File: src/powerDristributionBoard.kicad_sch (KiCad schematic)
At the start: 20 parts

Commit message: test
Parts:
- added D2: Light-Emitting Diode, symbol Simulation Generic Components:LED

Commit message: Test Commit
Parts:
- removed D1, D2: Light-Emitting Diode, symbol Simulation Generic Components:LED
- removed TVS3: Zener Diode, symbol Simulation Generic Components:Zener Diode
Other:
- removed sheet 26 to 12V(5A)1
- note added: "THIS SENTENCE IS BEING USED AS A TEST"
- moved on the sheet: D?, ESD1, ESD2, F?, M?, R1, R17, R18, R2, R9, TVS1, TVS2

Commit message: Testing to see if my updates get pushed to the repository.
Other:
- note added: "-Jonathan V"
- note added: "If you're reading this, that means my attempt to push updates into the repository was successful"
- note added: "P.S. Issac's the goat"
- note removed: "THIS SENTENCE IS BEING USED AS A TEST"
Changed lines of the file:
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@@
 	(generator_version "10.0")
 	(paper "A")
-	(text "THIS SENTENCE IS BEING USED AS A TEST"
+	(text "If you're reading this, that means my attempt to push updates into the repository was successful\n"
 		(exclude_from_sim no)
-		(at 86.868 45.72 0)
+		(at 121.158 26.416 0)
 		(effects
 			(font
@@
 			)
 		)
+	)
+	(text "-Jonathan V"
+		(exclude_from_sim no)
+		(at 214.63 34.036 0)
+		(effects
+			(font
+				(size 2.54 2.54)
+			)
+		)
+	)
+	(text "P.S. Issac's the goat"
+		(exclude_from_sim no)
+		(at 251.714 181.356 0)
+		(effects
+			(font
+				(size 1.27 1.27)
+			)
+		)

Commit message: Update power distribution board
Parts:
- removed D?: Light-Emitting Diode, symbol Simulation Generic Components:LED
- removed F?: MF-MSMF050-2, powerDristributionBoard-import-fps:BOUR-MF-MSMF050-2_V, symbol Autonomous Vehicle Lab:PPTC-2
- removed M?: P-channel Power MOSFET VDMOS Model, symbol Simulation Generic Components:MOSFET P-ch VDMOS
- removed R1, R2: Resistor, symbol Simulation Generic Components:Resistor
- removed TVS1: Zener Diode, symbol Simulation Generic Components:Zener Diode
- added D1: TVS, symbol Device:D_Zener
- added D2: LED, symbol Device:LED
- added F1: RTC, symbol Device:Fuse_Small
- added R1: Find Val, symbol Device:R_Small_US
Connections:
- net 26 to 12V(5A)/Vin+: now also D1.1 (K), F1.2, R1.1
- net GND: now also D1.2 (A), D2.1 (K)
- net Protection Circuit/Vout: now also F1.1
- new net: D2.2 (A), R1.2
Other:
- note removed: "-Jonathan V"
- note removed: "P.S. Issac's the goat"

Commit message: Added diode
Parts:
- added D3: TVS, symbol Device:D_Zener
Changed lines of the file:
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@@
+	)
+	(symbol
+		(lib_id "Device:D_Zener")
+		(at 68.58 127 270)
+		(unit 1)
+		(body_style 1)
+		(exclude_from_sim no)
+		(in_bom yes)
+		(on_board yes)
+		(in_pos_files yes)
+		(dnp no)
+		(fields_autoplaced yes)
+		(property "Reference" "D3"
+			(at 71.12 125.7299 90)
+			(show_name no)
+			(do_not_autoplace no)
+			(effects
+				(font
+					(size 1.27 1.27)
+				)
+				(justify left)
+			)
+		)
+		(property "Value" "TVS"
+			(at 71.12 128.2699 90)
+			(show_name no)
+			(do_not_autoplace no)
+			(effects
+				(font
+					(size 1.27 1.27)
+				)
+				(justify left)
+			)
+		)
+		(property "Footprint" ""
+			(at 68.58 127 0)
+			(hide yes)
+			(show_name no)
+			(do_not_autoplace no)
+			(effects
+				(font
+					(size 1.27 1.27)
+				)
+			)
+		)
+		(property "Datasheet" ""
+			(at 68.58 127 0)
+			(hide yes)
+			(show_name no)
+			(do_not_autoplace no)
+			(effects
+				(font
+					(size 1.27 1.27)
+				)
+			)
+		)
+		(property "Description" "Zener diode"
+			(at 68.58 127 0)
+			(hide yes)
+			(show_name no)
+			(do_not_autoplace no)
+			(effects
+				(font
+					(size 1.27 1.27)
+				)
+			)
+		)
+		(pin "1"
+		)
+		(pin "2"
+		)
+		(instances
+			(project "powerDristributionBoard"
+				(path "/d5fc2ae9-f21d-48b0-bd61-912ade1f672f"
+					(reference "D3")
+					(unit 1)
+				)
+			)
+		)
 	)
 	(symbol

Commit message: Added two diodes
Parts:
- added D4, D5: LED, symbol Device:LED
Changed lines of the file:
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@@
+	)
+	(symbol
+		(lib_id "Device:LED")
+		(at 106.68 124.46 90)
+		(unit 1)
+		(body_style 1)
+		(exclude_from_sim no)
+		(in_bom yes)
+		(on_board yes)
+		(in_pos_files yes)
+		(dnp no)
+		(fields_autoplaced yes)
+		(property "Reference" "D4"
+			(at 110.49 124.7774 90)
+			(show_name no)
+			(do_not_autoplace no)
+			(effects
+				(font
+					(size 1.27 1.27)
+				)
+				(justify right)
+			)
+		)
+		(property "Value" "LED"
+			(at 110.49 127.3174 90)
+			(show_name no)
+			(do_not_autoplace no)
+			(effects
+				(font
+					(size 1.27 1.27)
+				)
+				(justify right)
+			)
+		)
+		(property "Footprint" ""
+			(at 106.68 124.46 0)
+			(hide yes)
+			(show_name no)
+			(do_not_autoplace no)
+			(effects
+				(font
+					(size 1.27 1.27)
+				)
+			)
+		)
+		(property "Datasheet" ""
+			(at 106.68 124.46 0)
+			(hide yes)
+			(show_name no)
+			(do_not_autoplace no)
+			(effects
+				(font
+					(size 1.27 1.27)
+				)
+			)
+		)
+		(property "Description" "Light emitting diode"
+			(at 106.68 124.46 0)
+			(hide yes)
+			(show_name no)
+			(do_not_autoplace no)
+			(effects
+				(font
+					(size 1.27 1.27)
+				)
+			)
+		)
+		(property "Sim.Pins" "1=K 2=A"
+			(at 106.68 124.46 0)
+			(hide yes)
+			(show_name no)
+			(do_not_autoplace no)
+			(effects
+				(font
+					(size 1.27 1.27)
+				)
+			)
+		)
+		(pin "2"
+		)
+		(pin "1"
+		)
+		(instances
+			(project "powerDristributionBoard"
+				(path "/d5fc2ae9-f21d-48b0-bd61-912ade1f672f"
+					(reference "D4")
+					(unit 1)
+				)
+			)
+		)
 	)
 	(symbol
@@
 					(unit 1)
 				)
+			)
+		)
+	)
+	(symbol
+		(lib_id "Device:LED")
+		(at 111.76 124.46 90)
+		(unit 1)
+		(body_style 1)
+		(exclude_from_sim no)
+		(in_bom yes)
+		(on_board yes)
+		(in_pos_files yes)
+		(dnp no)
+		(fields_autoplaced yes)
+		(property "Reference" "D5"
+			(at 115.57 124.7774 90)
+			(show_name no)
+			(do_not_autoplace no)
+			(effects
+				(font
+					(size 1.27 1.27)
+				)
+				(justify right)
+			)
+		)
+		(property "Value" "LED"
+			(at 115.57 127.3174 90)
+			(show_name no)
+			(do_not_autoplace no)
+			(effects
+				(font
+					(size 1.27 1.27)
+				)
+				(justify right)
+			)
+		)
+		(property "Footprint" ""
+			(at 111.76 124.46 0)
+			(hide yes)
+			(show_name no)
+			(do_not_autoplace no)
+			(effects
+				(font
+					(size 1.27 1.27)
+				)
+			)
+		)
+		(property "Datasheet" ""
+			(at 111.76 124.46 0)
+			(hide yes)
+			(show_name no)
+			(do_not_autoplace no)
+			(effects
+				(font
+					(size 1.27 1.27)
+				)
+			)
+		)
+		(property "Description" "Light emitting diode"
+			(at 111.76 124.46 0)
+			(hide yes)
+			(show_name no)
+			(do_not_autoplace no)
+			(effects
+				(font
+					(size 1.27 1.27)
+				)
+			)
+		)
+		(property "Sim.Pins" "1=K 2=A"
+			(at 111.76 124.46 0)
+			(hide yes)
+			(show_name no)
+			(do_not_autoplace no)
+			(effects
+				(font
+					(size 1.27 1.27)
+				)
+			)
+		)
+		(pin "2"
+		)
+		(pin "1"
+		)
+		(instances
+			(project "powerDristributionBoard"
+				(path "/d5fc2ae9-f21d-48b0-bd61-912ade1f672f"
+					(reference "D5")
+					(unit 1)
+				)

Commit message: Test Updates - tst
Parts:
- removed D3: TVS, symbol Device:D_Zener
- removed D4, D5: LED, symbol Device:LED
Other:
- note added: "Another Test Update"
- note removed: "If you're reading this, that means my attempt to push updates into the repository was successful"

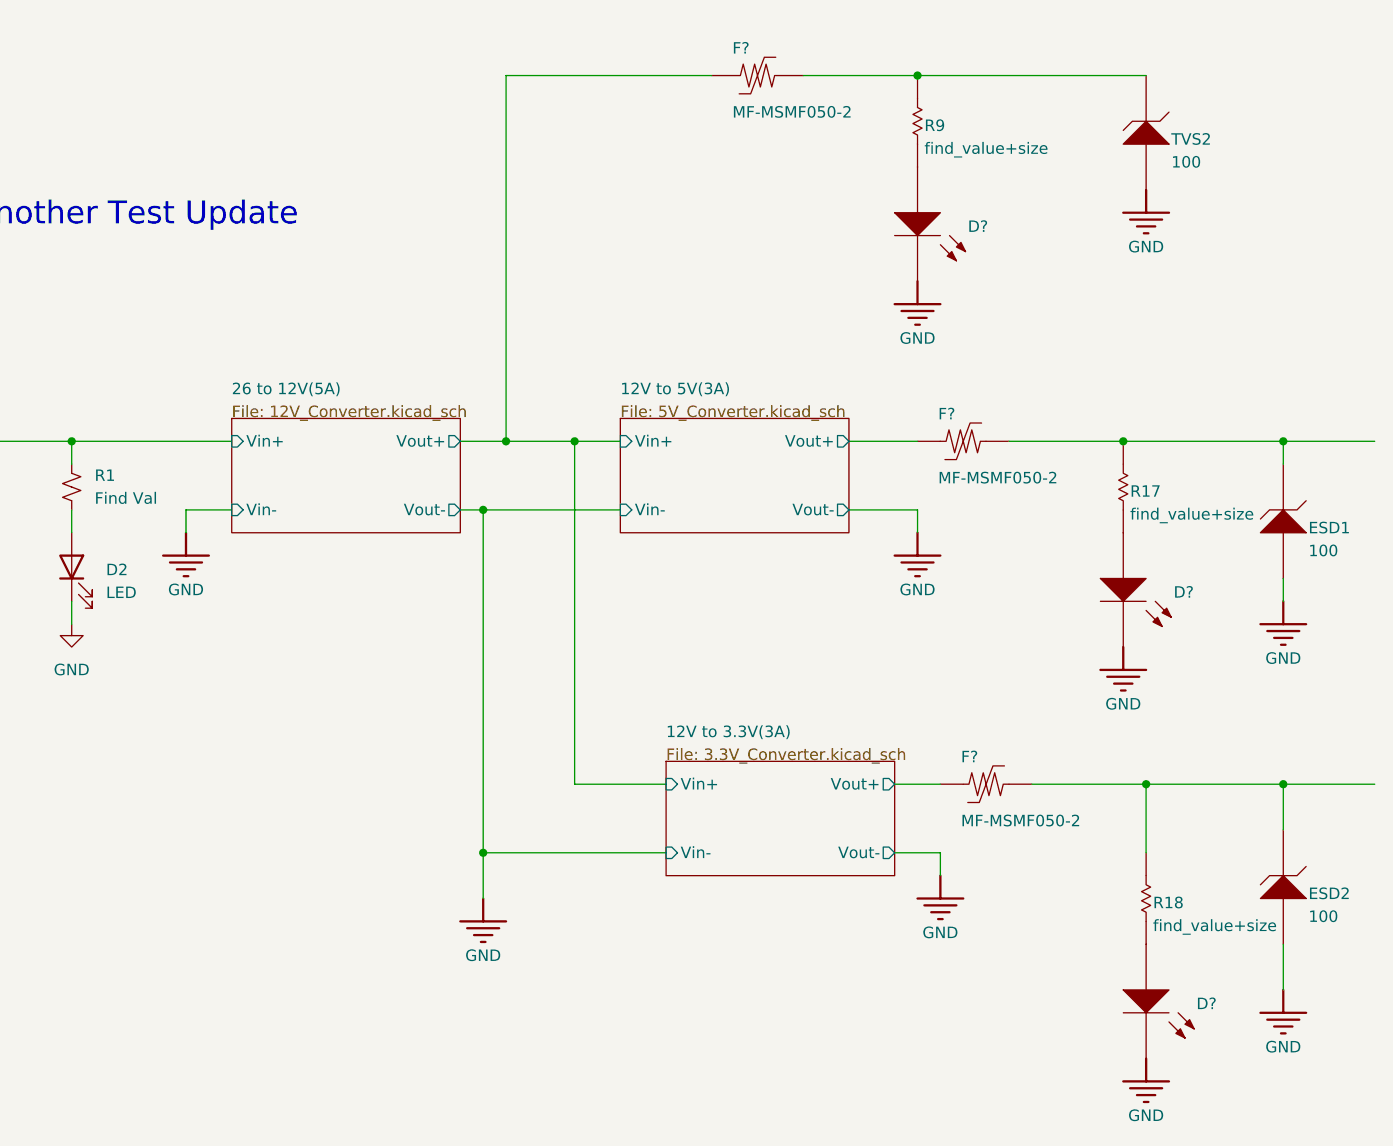
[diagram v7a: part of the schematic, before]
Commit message: Updated majority of passive components to KiCad format
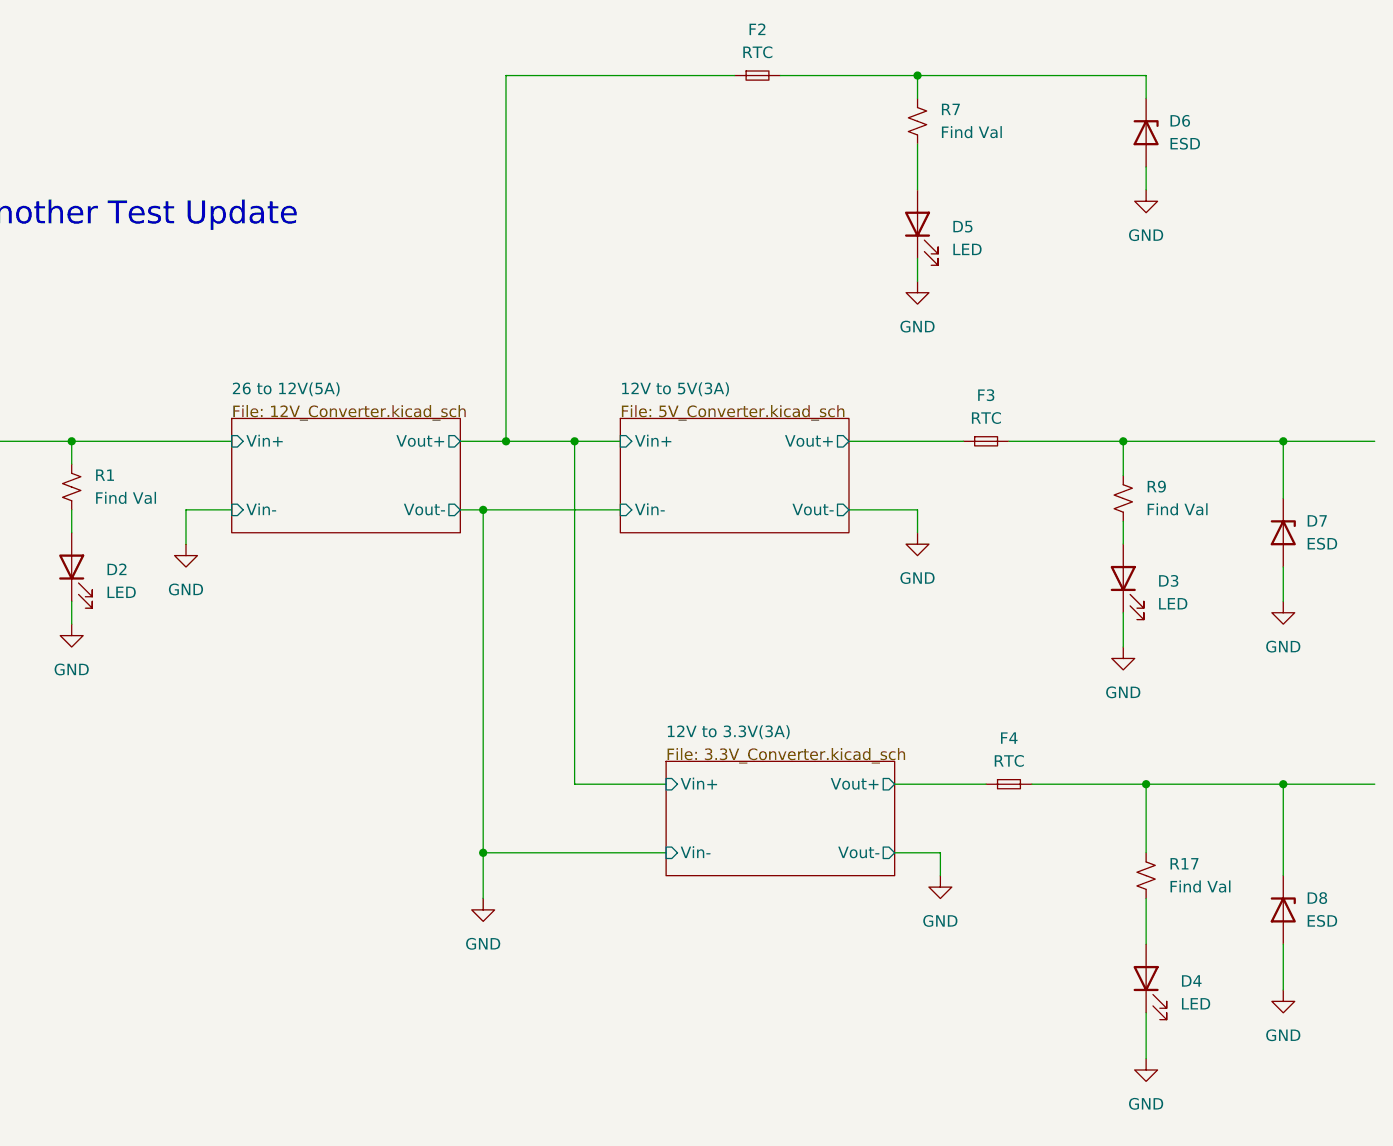
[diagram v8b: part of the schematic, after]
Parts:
- removed D? (x3): Light-Emitting Diode, symbol Simulation Generic Components:LED
- removed ESD1, ESD2, TVS2: Zener Diode, symbol Simulation Generic Components:Zener Diode
- removed F? (x3): MF-MSMF050-2, powerDristributionBoard-import-fps:BOUR-MF-MSMF050-2_V, symbol Autonomous Vehicle Lab:PPTC-2
- removed R17, R18, R9: Resistor, symbol Simulation Generic Components:Resistor
- added D3, D4, D5: LED, symbol Device:LED
- added D6, D7, D8: ESD, symbol Device:D_Zener
- added F2, F3, F4: RTC, symbol Device:Fuse_Small
- added R17, R7, R9: Find Val, symbol Device:R_Small_US
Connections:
- net 12V to 3.3V(3A)/Vin+: now also F2.1
- net 12V to 3.3V(3A)/Vout+: now also F4.1
- net 12V to 5V(3A)/Vout+: now also F3.1
- net GND: now also D3.1 (K), D4.1 (K), D5.1 (K), D6.2 (A), D7.2 (A), D8.2 (A)
- new net: D6.1 (K), F2.2, R7.1
- new net: D5.2 (A), R7.2
- new net: D7.1 (K), F3.2, R9.1
- new net: D3.2 (A), R9.2
- new net: D8.1 (K), F4.2, R17.1
- new net: D4.2 (A), R17.2
